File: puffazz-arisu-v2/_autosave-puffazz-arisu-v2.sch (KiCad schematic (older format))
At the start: 12 parts, among them SW1 SW_Push, U1 ATmega32U4-AU, Y1 16MHz

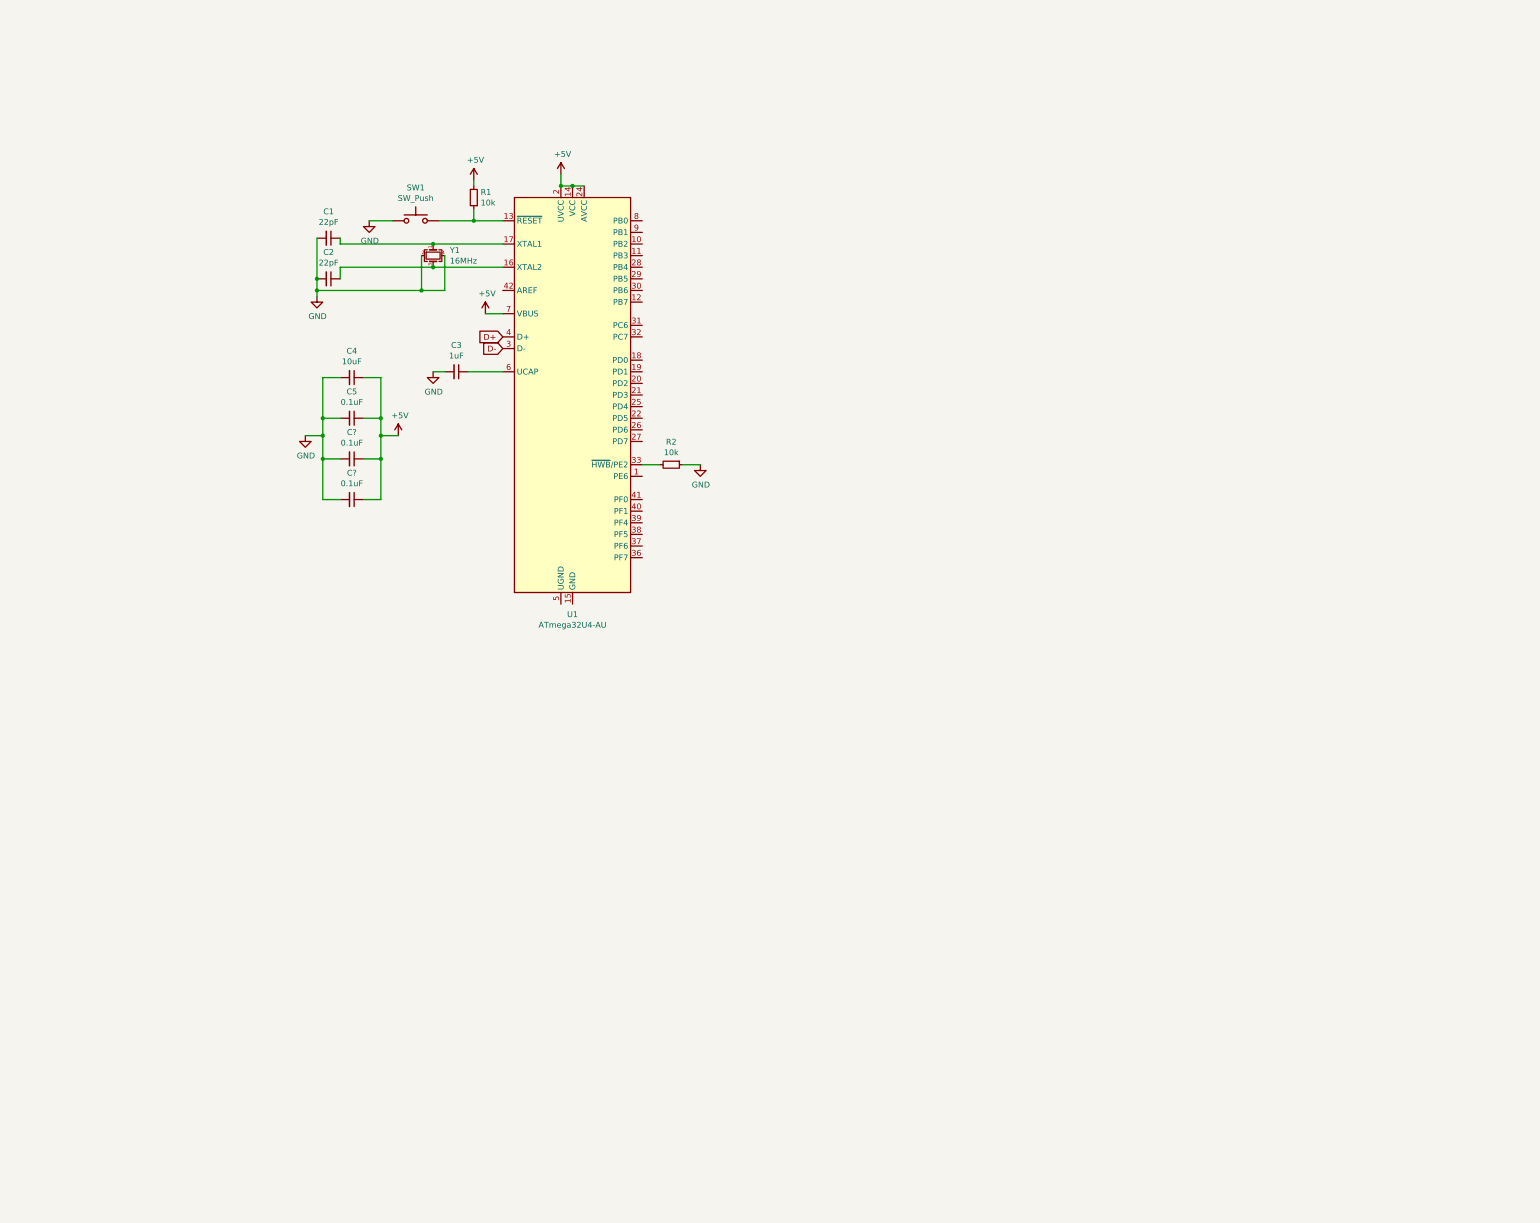
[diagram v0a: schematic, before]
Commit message: Completed full schematic draft without matrix labels on the MCU
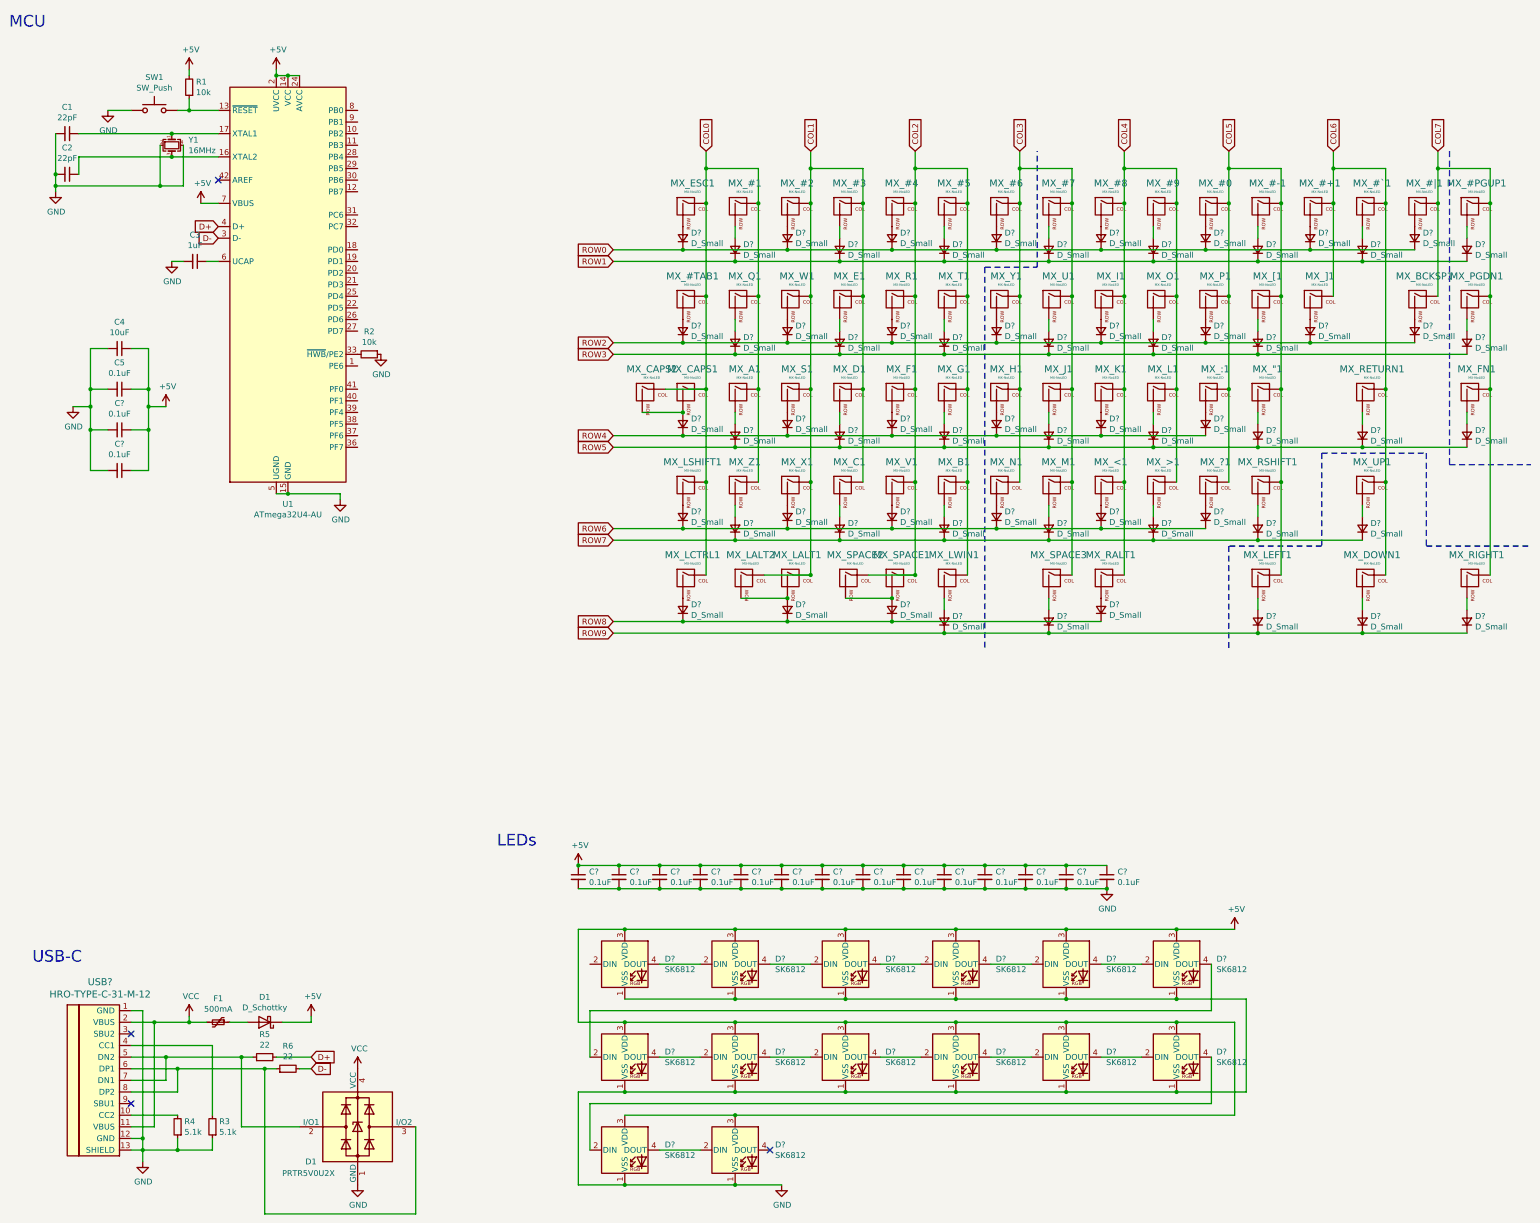
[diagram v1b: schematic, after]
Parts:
- added C? (x14): 0.1uF, symbol Device:C_Small
- added D1: D_Schottky, symbol Device:D_Schottky
- added D1: PRTR5V0U2X, Package_TO_SOT_SMD:SOT-143, symbol Power_Protection:PRTR5V0U2X
- added D? (x67): D_Small, symbol Device:D_Small
- added D? (x14): SK6812, LED_SMD:LED_SK6812_PLCC4_5.0x5.0mm_P3.2mm, symbol LED:SK6812
- added F1: 500mA, symbol Device:Polyfuse_Small
- added MX_"1, MX_#+1, MX_#-1, MX_#0, MX_#1, MX_#2, MX_#3, MX_#4, MX_#5, MX_#6, MX_#7, MX_#8, MX_#9, MX_#PGUP1, MX_#TAB1, MX_#`1, MX_#|1, MX_:1, MX_<1, MX_>1, MX_?1, MX_A1, MX_B1, MX_BCKSP1, MX_C1, MX_CAPS1, MX_CAPS2, MX_D1, MX_DOWN1, MX_E1, MX_ESC1, MX_F1, MX_FN1, MX_G1, MX_H1, MX_I1, MX_J1, MX_K1, MX_L1, MX_LALT1, MX_LALT2, MX_LCTRL1, MX_LEFT1, MX_LSHIFT1, MX_LWIN1, MX_M1, MX_N1, MX_O1, MX_P1, MX_PGDN1, MX_Q1, MX_R1, MX_RALT1, MX_RETURN1, MX_RIGHT1, MX_RSHIFT1, MX_S1, MX_SPACE1, MX_SPACE2, MX_SPACE3, MX_T1, MX_U1, MX_UP1, MX_V1, MX_W1, MX_X1, MX_Y1, MX_Z1, MX_[1, MX_]1: MX-NoLED, symbol MX_Alps_Hybrid:MX-NoLED
- added R3, R4: 5.1k, symbol Device:R_Small
- added R5, R6: 22, symbol Device:R_Small
- added USB?: HRO-TYPE-C-31-M-12, symbol Type-C:HRO-TYPE-C-31-M-12
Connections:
- net +5V: now also C?.1, C?.1, C?.1, C?.1, C?.1, C?.1, C?.1, C?.1, C?.1, C?.1, C?.1, C?.1, C?.1, C?.1, D1.1 (K), D?.3 (VDD), D?.3 (VDD), D?.3 (VDD), D?.3 (VDD), D?.3 (VDD), D?.3 (VDD), D?.3 (VDD), D?.3 (VDD), D?.3 (VDD), D?.3 (VDD), D?.3 (VDD), D?.3 (VDD), D?.3 (VDD), D?.3 (VDD)
- net D+: now also R5.2
- net D-: now also R6.2
- net GND: now also U1.15 (GND), U1.23 (GND), U1.35 (GND), U1.43 (GND), U1.5 (UGND), C?.2, C?.2, C?.2, C?.2, C?.2, C?.2, C?.2, C?.2, C?.2, C?.2, C?.2, C?.2, C?.2, C?.2, D1.1 (GND), D?.1 (VSS), D?.1 (VSS), D?.1 (VSS), D?.1 (VSS), D?.1 (VSS), D?.1 (VSS), D?.1 (VSS), D?.1 (VSS), D?.1 (VSS), D?.1 (VSS), D?.1 (VSS), D?.1 (VSS), D?.1 (VSS), D?.1 (VSS), R3.1, R4.1, USB?.1 (GND), USB?.12 (GND), USB?.13 (SHIELD)
- new net: D?.2 (A), MX_ESC1.2 (ROW)
- new net: D?.2 (A), MX_#1.2 (ROW)
- new net: D?.2 (A), MX_#2.2 (ROW)
- new net: D?.2 (A), MX_#3.2 (ROW)
- new net: D?.2 (A), MX_#4.2 (ROW)
- new net: D?.2 (A), MX_#5.2 (ROW)
- new net: D?.2 (A), MX_#6.2 (ROW)
- new net: D?.2 (A), MX_#7.2 (ROW)
- new net: D?.2 (A), MX_#8.2 (ROW)
- new net: D?.2 (A), MX_#9.2 (ROW)
- new net: D?.2 (A), MX_#0.2 (ROW)
- new net: D?.2 (A), MX_#-1.2 (ROW)
- new net: D?.2 (A), MX_#+1.2 (ROW)
- new net: R4.2, USB?.10 (CC2)
- new net: R3.2, USB?.4 (CC1)
- new net: D1.2 (I/O1), R5.1, USB?.5 (DN2), USB?.7 (DN1)
- new net: D1.3 (I/O2), R6.1, USB?.6 (DP1), USB?.8 (DP2)
- new net: D?.2 (A), MX_BCKSP1.2 (ROW)
- new net: D1.2 (A), F1.1
- new net: D?.2 (A), MX_#`1.2 (ROW)
- new net: D?.2 (A), MX_#|1.2 (ROW)
- new net: D?.2 (A), MX_#PGUP1.2 (ROW)
- new net: D?.2 (DIN), D?.4 (DOUT) (x13)
- new net: D?.2 (A), MX_#TAB1.2 (ROW)
- new net: D?.2 (A), MX_Q1.2 (ROW)
- new net: D?.2 (A), MX_W1.2 (ROW)
- new net: D?.2 (A), MX_E1.2 (ROW)
- new net: D?.2 (A), MX_R1.2 (ROW)
- new net: D?.2 (A), MX_T1.2 (ROW)
- new net: D?.2 (A), MX_Y1.2 (ROW)
- new net: D?.2 (A), MX_U1.2 (ROW)
- new net: D?.2 (A), MX_I1.2 (ROW)
- new net: D?.2 (A), MX_O1.2 (ROW)
- new net: D?.2 (A), MX_P1.2 (ROW)
- new net: D?.2 (A), MX_[1.2 (ROW)
- new net: D?.2 (A), MX_]1.2 (ROW)
- new net: D?.2 (A), MX_PGDN1.2 (ROW)
- new net: D?.2 (A), MX_RETURN1.2 (ROW)
- new net: D?.2 (A), MX_FN1.2 (ROW)
- new net: D?.2 (A), MX_K1.2 (ROW)
- new net: D?.2 (A), MX_L1.2 (ROW)
- new net: D?.2 (A), MX_:1.2 (ROW)
- new net: D?.2 (A), MX_"1.2 (ROW)
- new net: D?.2 (A), MX_F1.2 (ROW)
- new net: D?.2 (A), MX_G1.2 (ROW)
- new net: D?.2 (A), MX_H1.2 (ROW)
- new net: D?.2 (A), MX_J1.2 (ROW)
- new net: D?.2 (A), MX_CAPS1.2 (ROW), MX_CAPS2.2 (ROW)
- new net: D?.2 (A), MX_A1.2 (ROW)
- new net: D?.2 (A), MX_S1.2 (ROW)
- new net: D?.2 (A), MX_D1.2 (ROW)
- new net: D?.2 (A), MX_LSHIFT1.2 (ROW)
- new net: D?.2 (A), MX_Z1.2 (ROW)
- new net: D?.2 (A), MX_X1.2 (ROW)
- new net: D?.2 (A), MX_C1.2 (ROW)
- new net: D?.2 (A), MX_V1.2 (ROW)
- new net: D?.2 (A), MX_B1.2 (ROW)
- new net: D?.2 (A), MX_N1.2 (ROW)
- new net: D?.2 (A), MX_M1.2 (ROW)
- new net: D?.2 (A), MX_<1.2 (ROW)
- new net: D?.2 (A), MX_>1.2 (ROW)
- new net: D?.2 (A), MX_?1.2 (ROW)
- new net: D?.2 (A), MX_RSHIFT1.2 (ROW)
- new net: D?.2 (A), MX_UP1.2 (ROW)
- new net: D?.2 (A), MX_LEFT1.2 (ROW)
- new net: D?.2 (A), MX_DOWN1.2 (ROW)
- new net: D?.2 (A), MX_RIGHT1.2 (ROW)
- new net: D?.2 (A), MX_RALT1.2 (ROW)
- new net: D?.2 (A), MX_SPACE3.2 (ROW)
- new net: D?.2 (A), MX_LWIN1.2 (ROW)
- new net: D?.2 (A), MX_SPACE1.2 (ROW), MX_SPACE2.2 (ROW)
- new net: D?.2 (A), MX_LALT1.2 (ROW), MX_LALT2.2 (ROW)
- new net: D?.2 (A), MX_LCTRL1.2 (ROW)
- new net COL0: MX_#1.1 (COL), MX_#TAB1.1 (COL), MX_A1.1 (COL), MX_CAPS1.1 (COL), MX_CAPS2.1 (COL), MX_ESC1.1 (COL), MX_LCTRL1.1 (COL), MX_LSHIFT1.1 (COL), MX_Q1.1 (COL), MX_Z1.1 (COL)
- new net COL1: MX_#2.1 (COL), MX_#3.1 (COL), MX_C1.1 (COL), MX_D1.1 (COL), MX_E1.1 (COL), MX_LALT1.1 (COL), MX_LALT2.1 (COL), MX_S1.1 (COL), MX_W1.1 (COL), MX_X1.1 (COL)
- new net COL2: MX_#4.1 (COL), MX_#5.1 (COL), MX_B1.1 (COL), MX_F1.1 (COL), MX_G1.1 (COL), MX_LWIN1.1 (COL), MX_R1.1 (COL), MX_SPACE1.1 (COL), MX_SPACE2.1 (COL), MX_T1.1 (COL), MX_V1.1 (COL)
- new net COL3: MX_#6.1 (COL), MX_#7.1 (COL), MX_H1.1 (COL), MX_J1.1 (COL), MX_M1.1 (COL), MX_N1.1 (COL), MX_SPACE3.1 (COL), MX_U1.1 (COL), MX_Y1.1 (COL)
- new net COL4: MX_#8.1 (COL), MX_#9.1 (COL), MX_<1.1 (COL), MX_>1.1 (COL), MX_I1.1 (COL), MX_K1.1 (COL), MX_L1.1 (COL), MX_O1.1 (COL), MX_RALT1.1 (COL)
- new net COL5: MX_"1.1 (COL), MX_#-1.1 (COL), MX_#0.1 (COL), MX_:1.1 (COL), MX_?1.1 (COL), MX_LEFT1.1 (COL), MX_P1.1 (COL), MX_RSHIFT1.1 (COL), MX_[1.1 (COL)
- new net COL6: MX_#+1.1 (COL), MX_#`1.1 (COL), MX_DOWN1.1 (COL), MX_RETURN1.1 (COL), MX_UP1.1 (COL), MX_]1.1 (COL)
- new net COL7: MX_#PGUP1.1 (COL), MX_#|1.1 (COL), MX_BCKSP1.1 (COL), MX_FN1.1 (COL), MX_PGDN1.1 (COL), MX_RIGHT1.1 (COL)
- new net ROW0: D?.1 (K), D?.1 (K), D?.1 (K), D?.1 (K), D?.1 (K), D?.1 (K), D?.1 (K), D?.1 (K)
- new net ROW1: D?.1 (K), D?.1 (K), D?.1 (K), D?.1 (K), D?.1 (K), D?.1 (K), D?.1 (K), D?.1 (K)
- new net ROW2: D?.1 (K), D?.1 (K), D?.1 (K), D?.1 (K), D?.1 (K), D?.1 (K), D?.1 (K), D?.1 (K)
- new net ROW3: D?.1 (K), D?.1 (K), D?.1 (K), D?.1 (K), D?.1 (K), D?.1 (K), D?.1 (K)
- new net ROW4: D?.1 (K), D?.1 (K), D?.1 (K), D?.1 (K), D?.1 (K), D?.1 (K)
- new net ROW5: D?.1 (K), D?.1 (K), D?.1 (K), D?.1 (K), D?.1 (K), D?.1 (K), D?.1 (K), D?.1 (K)
- new net ROW6: D?.1 (K), D?.1 (K), D?.1 (K), D?.1 (K), D?.1 (K), D?.1 (K)
- new net ROW7: D?.1 (K), D?.1 (K), D?.1 (K), D?.1 (K), D?.1 (K), D?.1 (K), D?.1 (K)
- new net ROW8: D?.1 (K), D?.1 (K), D?.1 (K), D?.1 (K)
- new net ROW9: D?.1 (K), D?.1 (K), D?.1 (K), D?.1 (K), D?.1 (K)
- new net VCC: D1.4 (VCC), F1.2, USB?.11 (VBUS), USB?.2 (VBUS)
- no-connect marks 0 -> 4
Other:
- note added: "LEDs"
- note added: "MCU"
- note added: "USB-C"
- moved on the sheet: C1, C2, C3, C4, C5, C?, R1, R2, SW1, U1, Y1
